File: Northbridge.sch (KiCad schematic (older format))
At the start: 25 parts, among them J301 JTAG

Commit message: Redecoupling
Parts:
- removed C301, C302, C303, C304, C305, C306, C307, C308, C309, C310, C311, C312, C313, C314, C315, C316: 1u, IPC7351-Nominal:CAPC1005X55, symbol C-0402
- added C301, C302, C303, C304, C305, C306, C307, C308, C309, C310, C311, C312, C313, C314, C315, C316, C317, C318, C319, C320, C321, C322, C323, C324, C325, C326, C327, C328, C329, C330, C331, C332, C333, C334, C335, C336, C337, C338, C339, C340, C341, C342, C343, C344, C349, C350, C351, C352, C353, C354: 100n, IPC7351-Nominal:CAPC0603X33, symbol C-0201
- added C345, C346, C347, C348: 22u, IPC7351-Nominal:CAPC2012X70, symbol C-0805
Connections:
- wire segments 613 -> 721

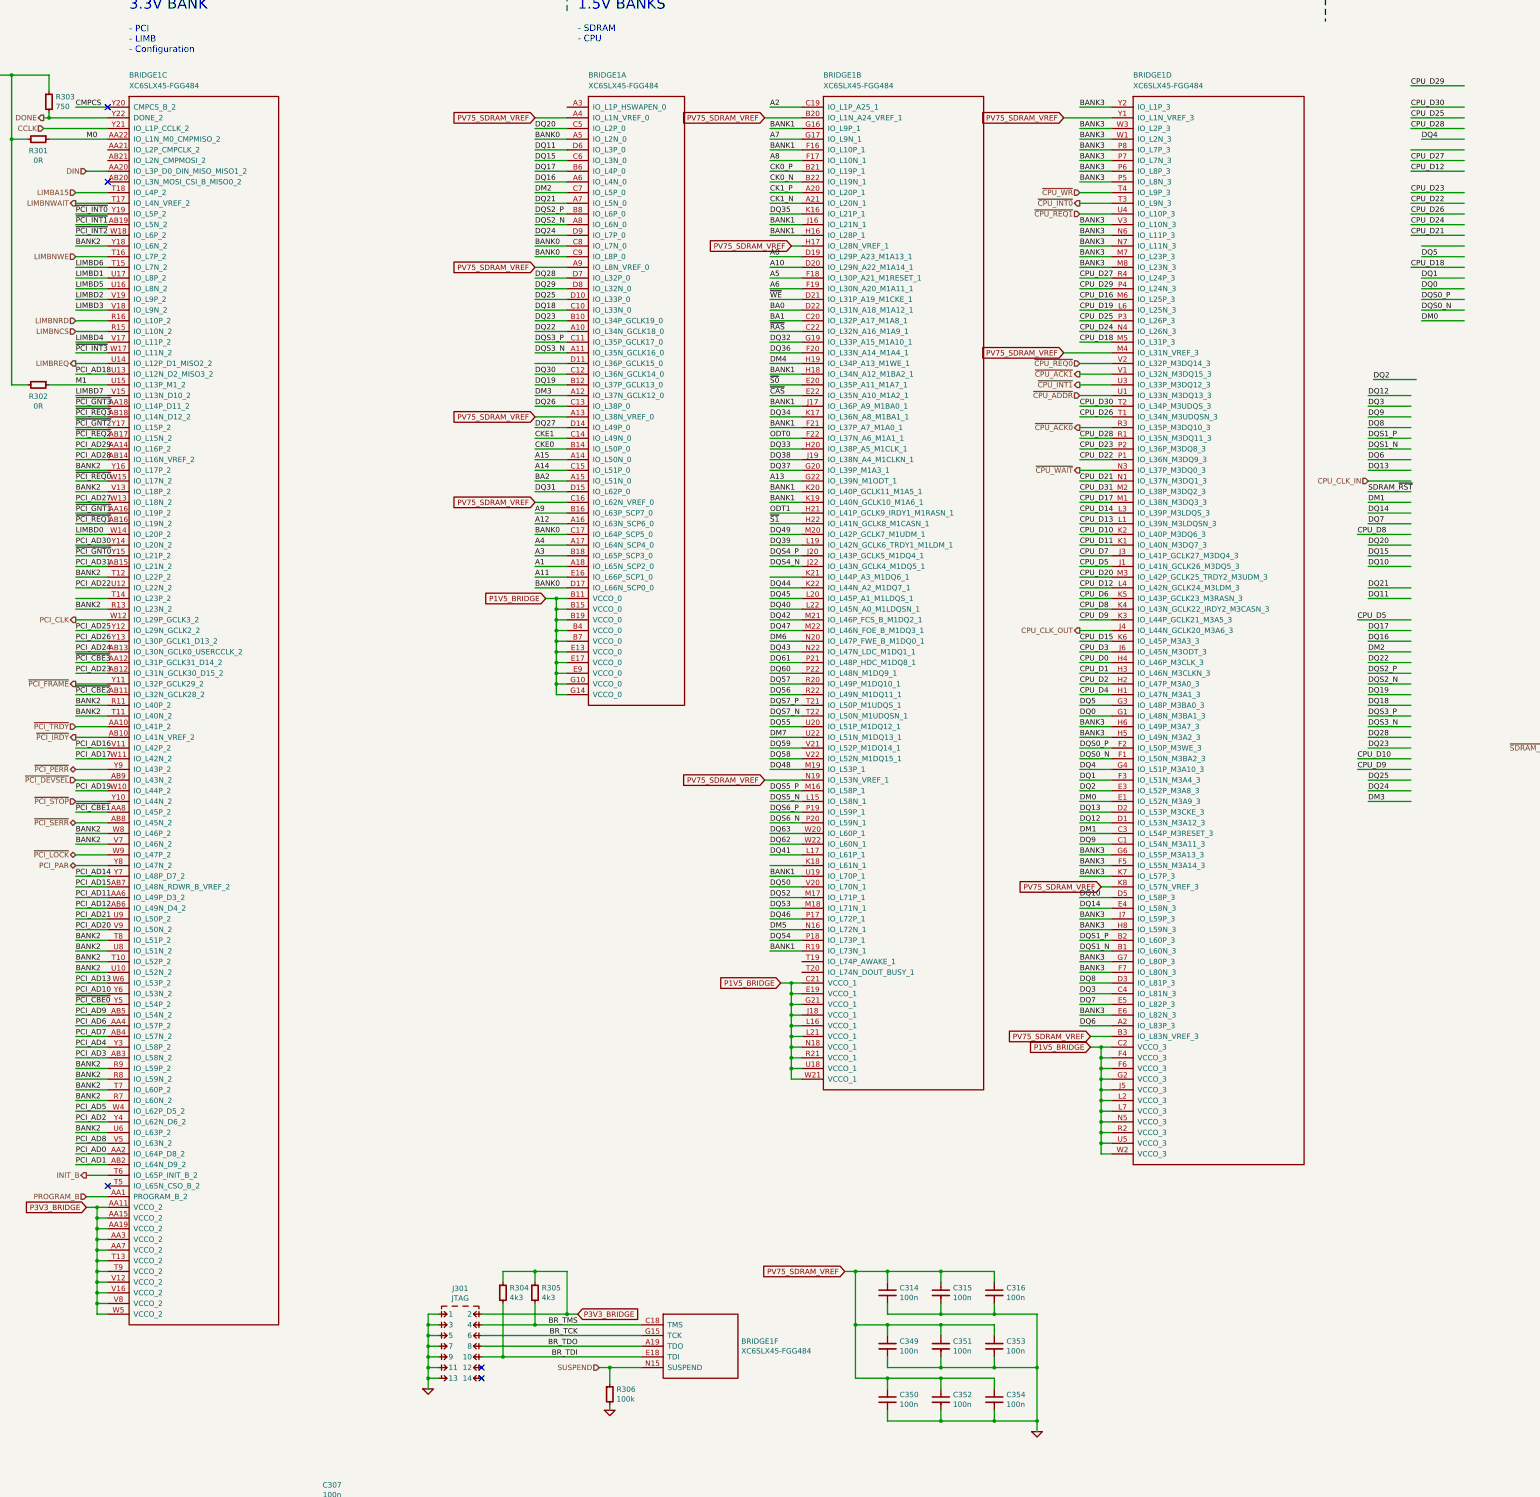
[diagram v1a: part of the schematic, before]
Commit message: Finish most redone routing
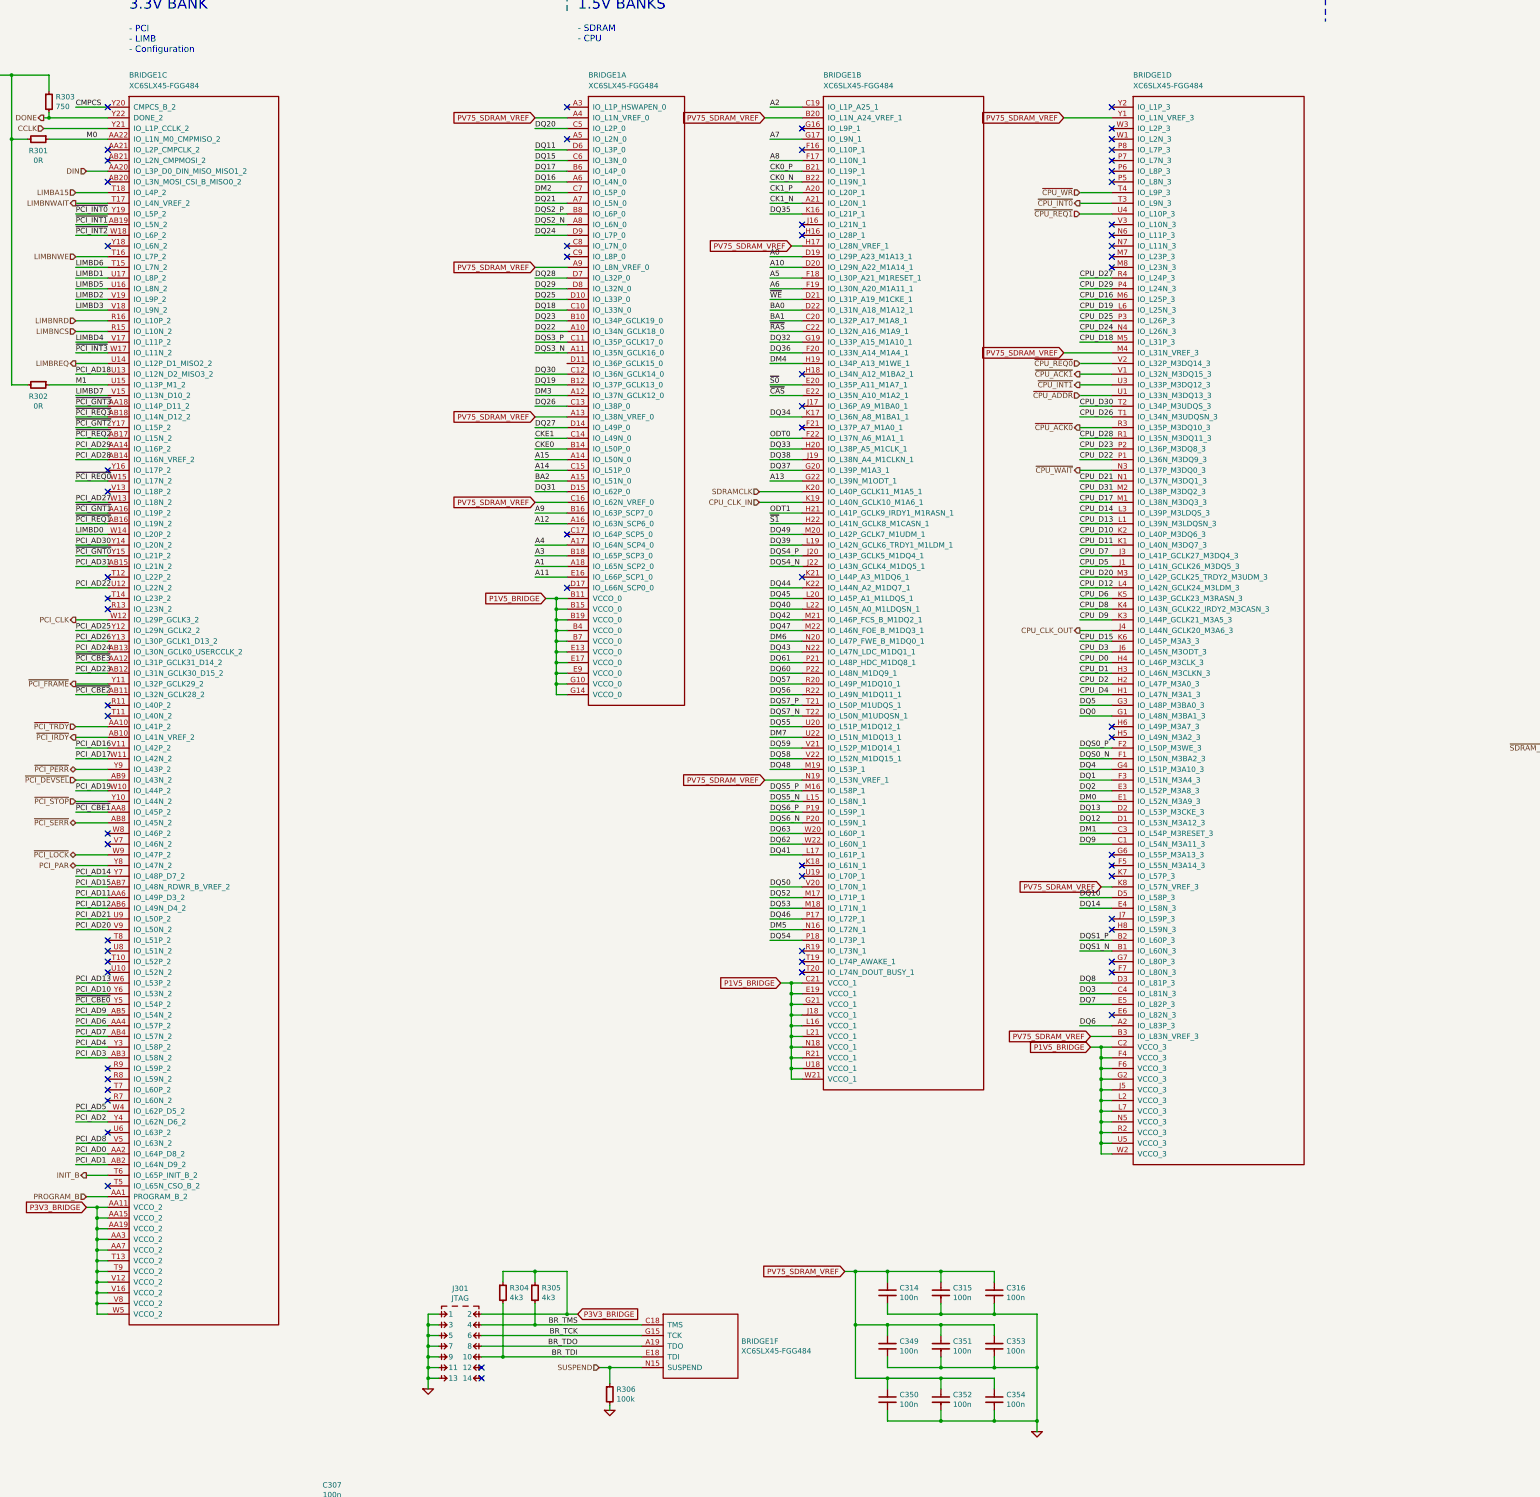
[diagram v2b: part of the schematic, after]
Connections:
- net labels added: SDRAMCLK
- net labels removed: BANK0, BANK1, BANK2, BANK3
- wire segments 721 -> 604
- no-connect marks 5 -> 67

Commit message: Fix more shit for to pass ERC
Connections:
- net SA0 is gone; now on net GND: SODIMM1.197 (SA0)
- net SA1 is gone; now on net GND: SODIMM1.201 (SA1)
- net DQ51: now also BRIDGE1.U19 (IO_L70P_1)
- net SDRAM_~RST renamed ~SDRAM_RST
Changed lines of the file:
@@
 Text Label 18000 8300 0    50   ~ 0
 ~S1
-Text Label 18000 8400 0    50   ~ 0
-SA0
-Text Label 18000 8500 0    50   ~ 0
-SA1
-Text Label 18000 8900 0    50   ~ 0
-SDRAM_~RST
 Text Label 18000 9200 0    50   ~ 0
 ODT0
@@
 P 6000 18200
 AR Path="/5763AB3B/5799D8FC" Ref="#PWR?"  Part="1"
-AR Path="/5763A638/5799D8FC" Ref="#PWR301"  Part="1"
-F 0 "#PWR301" H 6000 18200 30  0001 C CNN
+AR Path="/5763A638/5799D8FC" Ref="#PWR065"  Part="1"
+F 0 "#PWR065" H 6000 18200 30  0001 C CNN
 F 1 "GND" H 6000 18130 30  0001 C CNN
 F 2 "" H 6000 18200 60  0000 C CNN
@@
 P 7200 14800
 AR Path="/5763AB3B/57A7C581" Ref="#PWR?"  Part="1"
-AR Path="/5763A638/57A7C581" Ref="#PWR305"  Part="1"
-F 0 "#PWR305" H 7200 14800 30  0001 C CNN
+AR Path="/5763A638/57A7C581" Ref="#PWR066"  Part="1"
+F 0 "#PWR066" H 7200 14800 30  0001 C CNN
 F 1 "GND" H 7200 14730 30  0001 C CNN
 F 2 "" H 7200 14800 60  0000 C CNN
@@
 $EndComp
 $Comp
-L GND #PWR309
+L GND #PWR067
 U 1 1 57A6FC44
 P 8900 15000
-F 0 "#PWR309" H 8900 15000 30  0001 C CNN
+F 0 "#PWR067" H 8900 15000 30  0001 C CNN
 F 1 "GND" H 8900 14930 30  0001 C CNN
 F 2 "" H 8900 15000 60  0000 C CNN
@@
 	18000 8300 18500 8300
 Wire Wire Line
-	18000 8400 18500 8400
-Wire Wire Line
-	18000 8500 18500 8500
-Wire Wire Line
 	18000 9300 18500 9300
 Wire Wire Line
 	18000 9200 18500 9200
 Wire Wire Line
-	18000 8900 18500 8900
+	17900 8900 18500 8900
 Wire Notes Line
 	8500 1900 8500 1700
@@
 P 6000 19400
 AR Path="/5763AB3B/57C492A1" Ref="#PWR?"  Part="1"
-AR Path="/5763A638/57C492A1" Ref="#PWR302"  Part="1"
-F 0 "#PWR302" H 6000 19400 30  0001 C CNN
+AR Path="/5763A638/57C492A1" Ref="#PWR068"  Part="1"
+F 0 "#PWR068" H 6000 19400 30  0001 C CNN
 F 1 "GND" H 6000 19330 30  0001 C CNN
 F 2 "" H 6000 19400 60  0000 C CNN
@@
 P 6000 20600
 AR Path="/5763AB3B/57C49506" Ref="#PWR?"  Part="1"
-AR Path="/5763A638/57C49506" Ref="#PWR303"  Part="1"
-F 0 "#PWR303" H 6000 20600 30  0001 C CNN
+AR Path="/5763A638/57C49506" Ref="#PWR069"  Part="1"
+F 0 "#PWR069" H 6000 20600 30  0001 C CNN
 F 1 "GND" H 6000 20530 30  0001 C CNN
 F 2 "" H 6000 20600 60  0000 C CNN
@@
 P 8600 18200
 AR Path="/5763AB3B/57C4D6CE" Ref="#PWR?"  Part="1"
-AR Path="/5763A638/57C4D6CE" Ref="#PWR307"  Part="1"
-F 0 "#PWR307" H 8600 18200 30  0001 C CNN
+AR Path="/5763A638/57C4D6CE" Ref="#PWR070"  Part="1"
+F 0 "#PWR070" H 8600 18200 30  0001 C CNN
 F 1 "GND" H 8600 18130 30  0001 C CNN
 F 2 "" H 8600 18200 60  0000 C CNN
@@
 P 8600 19400
 AR Path="/5763AB3B/57C4DA02" Ref="#PWR?"  Part="1"
-AR Path="/5763A638/57C4DA02" Ref="#PWR308"  Part="1"
-F 0 "#PWR308" H 8600 19400 30  0001 C CNN
+AR Path="/5763A638/57C4DA02" Ref="#PWR071"  Part="1"
+F 0 "#PWR071" H 8600 19400 30  0001 C CNN
 F 1 "GND" H 8600 19330 30  0001 C CNN
 F 2 "" H 8600 19400 60  0000 C CNN
@@
 P 7900 20200
 AR Path="/5763AB3B/57C5B80A" Ref="#PWR?"  Part="1"
-AR Path="/5763A638/57C5B80A" Ref="#PWR306"  Part="1"
-F 0 "#PWR306" H 7900 20200 30  0001 C CNN
+AR Path="/5763A638/57C5B80A" Ref="#PWR072"  Part="1"
+F 0 "#PWR072" H 7900 20200 30  0001 C CNN
 F 1 "GND" H 7900 20130 30  0001 C CNN
 F 2 "" H 7900 20200 60  0000 C CNN
@@
 P 7000 20700
 AR Path="/5763AB3B/57C5BDEC" Ref="#PWR?"  Part="1"
-AR Path="/5763A638/57C5BDEC" Ref="#PWR304"  Part="1"
-F 0 "#PWR304" H 7000 20700 30  0001 C CNN
+AR Path="/5763A638/57C5BDEC" Ref="#PWR073"  Part="1"
+F 0 "#PWR073" H 7000 20700 30  0001 C CNN
 F 1 "GND" H 7000 20630 30  0001 C CNN
 F 2 "" H 7000 20700 60  0000 C CNN
@@
 Connection ~ 12500 14600
 $Comp
-L GND #PWR310
+L GND #PWR074
 U 1 1 57C62AB6
 P 12900 15200
-F 0 "#PWR310" H 12900 15200 30  0001 C CNN
+F 0 "#PWR074" H 12900 15200 30  0001 C CNN
 F 1 "GND" H 12900 15130 30  0001 C CNN
 F 2 "" H 12900 15200 60  0000 C CNN
@@
 NoConn ~ 8500 7300
 NoConn ~ 10700 9900
-NoConn ~ 10700 10000
 NoConn ~ 10700 10700
 NoConn ~ 10700 10800
@@
 Wire Wire Line
 	10700 6400 10300 6400
+Text Label 10400 10000 0    50   ~ 0
+DQ51
+Wire Wire Line
+	10700 10000 10400 10000
+$Comp
+L GND #PWR075
+U 1 1 57C95A90
+P 18400 8550
+F 0 "#PWR075" H 18400 8550 30  0001 C CNN
+F 1 "GND" H 18400 8480 30  0001 C CNN
+F 2 "" H 18400 8550 60  0000 C CNN
+F 3 "" H 18400 8550 60  0000 C CNN
+	1    18400 8550
+	1    0    0    -1
+$EndComp
+Wire Wire Line
+	18400 8550 18400 8400
+Wire Wire Line
+	18400 8400 18500 8400
+Wire Wire Line
+	18500 8500 18400 8500
+Connection ~ 18400 8500
+Text HLabel 17900 8900 0    50   Input ~ 0
+~SDRAM_RST
+NoConn ~ 8500 5200
 $EndSCHEMATC

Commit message: Fix fuckup 2: bank 0 ain't got no SSTL
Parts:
- removed C349, C350, C351, C354: 100n, IPC7351-Nominal:CAPC0603X33, symbol C-0201
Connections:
- net A1: now also BRIDGE1.E5 (IO_L82P_3); no longer BRIDGE1.A18 (IO_L65N_SCP2_0)
- net A11: now also BRIDGE1.C1 (IO_L54N_M3A11_3); no longer BRIDGE1.E16 (IO_L66P_SCP1_0)
- net A12: now also BRIDGE1.B2 (IO_L60P_3); no longer BRIDGE1.A16 (IO_L63N_SCP6_0)
- net A14: now also BRIDGE1.D2 (IO_L53P_M3CKE_3); no longer BRIDGE1.C15 (IO_L51P_0)
- net A15: now also BRIDGE1.D1 (IO_L53N_M3A12_3); no longer BRIDGE1.A14 (IO_L50N_0)
- net A3: now also BRIDGE1.E4 (IO_L58N_3); no longer BRIDGE1.B18 (IO_L65P_SCP3_0)
- net A4: now also BRIDGE1.G4 (IO_L51P_M3A10_3); no longer BRIDGE1.A17 (IO_L64N_SCP4_0)
- net A9: now also BRIDGE1.A2 (IO_L83P_3); no longer BRIDGE1.B16 (IO_L63P_SCP7_0)
- net BA2: now also BRIDGE1.B1 (IO_L60N_3); no longer BRIDGE1.A15 (IO_L51N_0)
- net CKE0: now also BRIDGE1.C3 (IO_L54P_M3RESET_3); no longer BRIDGE1.B14 (IO_L50P_0)
- net CKE1: now also BRIDGE1.E1 (IO_L52N_M3A9_3); no longer BRIDGE1.C14 (IO_L49N_0)
- net CPU_CLK_OUT: now also BRIDGE1.A9 (IO_L8N_VREF_0); no longer BRIDGE1.J4 (IO_L44N_GCLK20_M3A6_3)
- net CPU_D0: now also BRIDGE1.C11 (IO_L35P_GCLK17_0); no longer BRIDGE1.H4 (IO_L46P_M3CLK_3)
- net CPU_D1: now also BRIDGE1.A11 (IO_L35N_GCLK16_0); no longer BRIDGE1.H3 (IO_L46N_M3CLKN_3)
- net CPU_D10: now also BRIDGE1.E16 (IO_L66P_SCP1_0); no longer BRIDGE1.K2 (IO_L40P_M3DQ6_3)
- net CPU_D11: now also BRIDGE1.C15 (IO_L51P_0); no longer BRIDGE1.K1 (IO_L40N_M3DQ7_3)
- net CPU_D12: now also BRIDGE1.B8 (IO_L6P_0); no longer BRIDGE1.L4 (IO_L42N_GCLK24_M3LDM_3)
- net CPU_D13: now also BRIDGE1.A7 (IO_L5N_0); no longer BRIDGE1.L1 (IO_L39N_M3LDQSN_3)
- net CPU_D14: now also BRIDGE1.D15 (IO_L62P_0); no longer BRIDGE1.L3 (IO_L39P_M3LDQS_3)
- net CPU_D15: now also BRIDGE1.A6 (IO_L4N_0); no longer BRIDGE1.K6 (IO_L45P_M3A3_3)
- net CPU_D16: now also BRIDGE1.B6 (IO_L4P_0); no longer BRIDGE1.M6 (IO_L25P_3)
- net CPU_D17: now also BRIDGE1.A5 (IO_L2N_0); no longer BRIDGE1.M1 (IO_L38N_M3DQ3_3)
- net CPU_D18: now also BRIDGE1.A4 (IO_L1N_VREF_0); no longer BRIDGE1.M5 (IO_L31P_3)
- net CPU_D19: now also BRIDGE1.D14 (IO_L49P_0); no longer BRIDGE1.L6 (IO_L25N_3)
- net CPU_D2: now also BRIDGE1.A16 (IO_L63N_SCP6_0); no longer BRIDGE1.H2 (IO_L47P_M3A0_3)
- net CPU_D20: now also BRIDGE1.C13 (IO_L38P_0); no longer BRIDGE1.M3 (IO_L42P_GCLK25_TRDY2_M3UDM_3)
- net CPU_D21: now also BRIDGE1.A3 (IO_L1P_HSWAPEN_0); no longer BRIDGE1.N1 (IO_L37N_M3DQ1_3)
- net CPU_D22: now also BRIDGE1.D3 (IO_L81P_3); no longer BRIDGE1.P1 (IO_L36N_M3DQ9_3)
- net CPU_D23: now also BRIDGE1.D9 (IO_L7P_0); no longer BRIDGE1.P2 (IO_L36P_M3DQ8_3)
- net CPU_D24: now also BRIDGE1.C10 (IO_L33N_0); no longer BRIDGE1.N4 (IO_L26N_3)
- net CPU_D25: now also BRIDGE1.E3 (IO_L52P_M3A8_3); no longer BRIDGE1.P3 (IO_L26P_3)
- net CPU_D26: now also BRIDGE1.C8 (IO_L7N_0); no longer BRIDGE1.T1 (IO_L34N_M3UDQSN_3)
- net CPU_D27: now also BRIDGE1.D8 (IO_L32N_0); no longer BRIDGE1.R4 (IO_L24P_3)
- net CPU_D28: now also BRIDGE1.F2 (IO_L50P_M3WE_3); no longer BRIDGE1.R1 (IO_L35N_M3DQ11_3)
- net CPU_D29: now also BRIDGE1.C9 (IO_L8P_0); no longer BRIDGE1.P4 (IO_L24N_3)
- net CPU_D3: now also BRIDGE1.A10 (IO_L34N_GCLK18_0); no longer BRIDGE1.J6 (IO_L45N_M3ODT_3)
- net CPU_D30: now also BRIDGE1.K6 (IO_L45P_M3A3_3); no longer BRIDGE1.T2 (IO_L34P_M3UDQS_3)
- net CPU_D31: now also BRIDGE1.D11 (IO_L36P_GCLK15_0); no longer BRIDGE1.M2 (IO_L38P_M3DQ2_3)
- net CPU_D4: now also BRIDGE1.A15 (IO_L51N_0); no longer BRIDGE1.H1 (IO_L47N_M3A1_3)
- net CPU_D5: now also BRIDGE1.B10 (IO_L34P_GCLK19_0); no longer BRIDGE1.J1 (IO_L41N_GCLK26_M3DQ5_3)
- net CPU_D6: now also BRIDGE1.C14 (IO_L49N_0); no longer BRIDGE1.K5 (IO_L43P_GCLK23_M3RASN_3)
- net CPU_D7: now also BRIDGE1.D17 (IO_L66N_SCP0_0); no longer BRIDGE1.J3 (IO_L41P_GCLK27_M3DQ4_3)
- net CPU_D8: now also BRIDGE1.C16 (IO_L62N_VREF_0); no longer BRIDGE1.K4 (IO_L43N_GCLK22_IRDY2_M3CASN_3)
- net CPU_D9: now also BRIDGE1.A8 (IO_L6N_0); no longer BRIDGE1.K3 (IO_L44P_GCLK21_M3A5_3)
- net DM0: now also BRIDGE1.U1 (IO_L33N_M3DQ13_3); no longer BRIDGE1.E1 (IO_L52N_M3A9_3)
- net DM1: now also BRIDGE1.R4 (IO_L24P_3); no longer BRIDGE1.C3 (IO_L54P_M3RESET_3)
- net DM2: now also BRIDGE1.K2 (IO_L40P_M3DQ6_3); no longer BRIDGE1.C7 (IO_L5P_0)
- net DM3: now also BRIDGE1.H5 (IO_L49N_M3A2_3); no longer BRIDGE1.A12 (IO_L37N_GCLK12_0)
- net DQ0: now also BRIDGE1.W3 (IO_L2P_3); no longer BRIDGE1.G1 (IO_L48N_M3BA1_3)
- net DQ1: now also BRIDGE1.V1 (IO_L32N_M3DQ15_3); no longer BRIDGE1.F3 (IO_L51N_M3A4_3)
- net DQ10: now also BRIDGE1.P3 (IO_L26P_3); no longer BRIDGE1.D5 (IO_L58P_3)
- net DQ11: now also BRIDGE1.P5 (IO_L8N_3); no longer BRIDGE1.D6 (IO_L3P_0)
- net DQ12: now also BRIDGE1.U4 (IO_L10P_3); no longer BRIDGE1.D1 (IO_L53N_M3A12_3)
- net DQ13: now also BRIDGE1.U3 (IO_L33P_M3DQ12_3); no longer BRIDGE1.D2 (IO_L53P_M3CKE_3)
- net DQ14: now also BRIDGE1.P4 (IO_L24N_3); no longer BRIDGE1.E4 (IO_L58N_3)
- net DQ15: now also BRIDGE1.N4 (IO_L26N_3); no longer BRIDGE1.C6 (IO_L3N_0)
- net DQ16: now also BRIDGE1.M2 (IO_L38P_M3DQ2_3); no longer BRIDGE1.A6 (IO_L4N_0)
- net DQ17: now also BRIDGE1.L1 (IO_L39N_M3LDQSN_3); no longer BRIDGE1.B6 (IO_L4P_0)
- net DQ18: now also BRIDGE1.G1 (IO_L48N_M3BA1_3); no longer BRIDGE1.C10 (IO_L33N_0)
- net DQ19: now also BRIDGE1.F1 (IO_L50N_M3BA2_3); no longer BRIDGE1.B12 (IO_L37P_GCLK13_0)
- net DQ2: now also BRIDGE1.V2 (IO_L32P_M3DQ14_3); no longer BRIDGE1.E3 (IO_L52P_M3A8_3)
- net DQ20: now also BRIDGE1.M1 (IO_L38N_M3DQ3_3); no longer BRIDGE1.C5 (IO_L2P_0)
- net DQ21: now also BRIDGE1.K1 (IO_L40N_M3DQ7_3); no longer BRIDGE1.A7 (IO_L5N_0)
- net DQ22: now also BRIDGE1.H1 (IO_L47N_M3A1_3); no longer BRIDGE1.A10 (IO_L34N_GCLK18_0)
- net DQ23: now also BRIDGE1.H2 (IO_L47P_M3A0_3); no longer BRIDGE1.B10 (IO_L34P_GCLK19_0)
- net DQ24: now also BRIDGE1.L4 (IO_L42N_GCLK24_M3LDM_3); no longer BRIDGE1.D9 (IO_L7P_0)
- net DQ25: now also BRIDGE1.L3 (IO_L39P_M3LDQS_3); no longer BRIDGE1.D10 (IO_L33P_0)
- net DQ26: now also BRIDGE1.H3 (IO_L46N_M3CLKN_3); no longer BRIDGE1.C13 (IO_L38P_0)
- net DQ27: now also BRIDGE1.G3 (IO_L48P_M3BA0_3); no longer BRIDGE1.D14 (IO_L49P_0)
- net DQ28: now also BRIDGE1.N3 (IO_L37P_M3DQ0_3); no longer BRIDGE1.D7 (IO_L32P_0)
- net DQ29: now also BRIDGE1.M3 (IO_L42P_GCLK25_TRDY2_M3UDM_3); no longer BRIDGE1.D8 (IO_L32N_0)
- net DQ3: now also BRIDGE1.P2 (IO_L36P_M3DQ8_3); no longer BRIDGE1.C4 (IO_L81N_3)
- net DQ30: now also BRIDGE1.J4 (IO_L44N_GCLK20_M3A6_3); no longer BRIDGE1.C12 (IO_L36N_GCLK14_0)
- net DQ31: now also BRIDGE1.H4 (IO_L46P_M3CLK_3); no longer BRIDGE1.D15 (IO_L62P_0)
- net DQ4: now also BRIDGE1.W1 (IO_L2N_3); no longer BRIDGE1.G4 (IO_L51P_M3A10_3)
- net DQ5: now also BRIDGE1.V3 (IO_L10N_3); no longer BRIDGE1.G3 (IO_L48P_M3BA0_3)
- net DQ6: now also BRIDGE1.P1 (IO_L36N_M3DQ9_3); no longer BRIDGE1.A2 (IO_L83P_3)
- net DQ7: now also BRIDGE1.N1 (IO_L37N_M3DQ1_3); no longer BRIDGE1.E5 (IO_L82P_3)
- net DQ8: now also BRIDGE1.T4 (IO_L9P_3); no longer BRIDGE1.D3 (IO_L81P_3)
- net DQ9: now also BRIDGE1.T3 (IO_L9N_3); no longer BRIDGE1.C1 (IO_L54N_M3A11_3)
- net DQS0_N: now also BRIDGE1.T1 (IO_L34N_M3UDQSN_3); no longer BRIDGE1.F1 (IO_L50N_M3BA2_3)
- net DQS0_P: now also BRIDGE1.T2 (IO_L34P_M3UDQS_3); no longer BRIDGE1.F2 (IO_L50P_M3WE_3)
- net DQS1_N: now also BRIDGE1.R1 (IO_L35N_M3DQ11_3); no longer BRIDGE1.B1 (IO_L60N_3)
- net DQS1_P: now also BRIDGE1.R3 (IO_L35P_M3DQ10_3); no longer BRIDGE1.B2 (IO_L60P_3)
- net DQS2_N: now also BRIDGE1.J1 (IO_L41N_GCLK26_M3DQ5_3); no longer BRIDGE1.A8 (IO_L6N_0)
- net DQS2_P: now also BRIDGE1.J3 (IO_L41P_GCLK27_M3DQ4_3); no longer BRIDGE1.B8 (IO_L6P_0)
- net DQS3_N: now also BRIDGE1.K4 (IO_L43N_GCLK22_IRDY2_M3CASN_3); no longer BRIDGE1.A11 (IO_L35N_GCLK16_0)
- net DQS3_P: now also BRIDGE1.K5 (IO_L43P_GCLK23_M3RASN_3); no longer BRIDGE1.C11 (IO_L35P_GCLK17_0)
- net PV75_SDRAM_VREF: no longer BRIDGE1.A13 (IO_L38N_VREF_0), BRIDGE1.A4 (IO_L1N_VREF_0), BRIDGE1.A9 (IO_L8N_VREF_0), BRIDGE1.C16 (IO_L62N_VREF_0)
- net ~CPU_ACK0: now also BRIDGE1.F3 (IO_L51N_M3A4_3); no longer BRIDGE1.R3 (IO_L35P_M3DQ10_3)
- net ~CPU_ACK1: now also BRIDGE1.M5 (IO_L31P_3); no longer BRIDGE1.V1 (IO_L32N_M3DQ15_3)
- net ~CPU_ADDR: now also BRIDGE1.C7 (IO_L5P_0); no longer BRIDGE1.U1 (IO_L33N_M3DQ13_3)
- net ~CPU_INT0: now also BRIDGE1.L6 (IO_L25N_3); no longer BRIDGE1.T3 (IO_L9N_3)
- net ~CPU_INT1: now also BRIDGE1.N6 (IO_L11P_3); no longer BRIDGE1.U3 (IO_L33P_M3DQ12_3)
- net ~CPU_REQ0: now also BRIDGE1.C6 (IO_L3N_0); no longer BRIDGE1.V2 (IO_L32P_M3DQ14_3)
- net ~CPU_REQ1: now also BRIDGE1.D6 (IO_L3P_0); no longer BRIDGE1.U4 (IO_L10P_3)
- net ~CPU_WAIT: now also BRIDGE1.D10 (IO_L33P_0); no longer BRIDGE1.N3 (IO_L37P_M3DQ0_3)
- net ~CPU_WR: now also BRIDGE1.D7 (IO_L32P_0); no longer BRIDGE1.T4 (IO_L9P_3)
- no-connect marks 67 -> 71

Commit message: Tidy schematics and produce PDF
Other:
- moved on the sheet: BRIDGE1A, BRIDGE1B, BRIDGE1C, BRIDGE1D, BRIDGE1F, C301, C302, C303, C304, C305, C306, C307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

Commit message: Update for KiCad 5
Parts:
- BRIDGE1: symbol XC6SLX45-FGG484 -> Xilinx:XC6SLX45-FGG484
- C301, C302, C303, C304, C305, C306, C307, C308, C309, C310, C311, C312, C313, C314, C315, C316, C317, C318, C319, C320, C321, C322, C323, C324, C325, C326, C327, C328, C329, C330, C331, C332, C333, C334, C335, C336, C337, C338, C339, C340, C341, C342, C343, C344, C352, C353: symbol C-0201 -> pasv-cap:C-0201
- C345, C346, C347, C348: symbol C-0805 -> pasv-cap:C-0805
- J301: symbol CONN-100MIL-M-2x7-SHROUD -> conn-100mil:CONN-100MIL-M-2x7-SHROUD
- R301, R302, R303, R304, R305, R306: symbol R-0402 -> pasv-res:R-0402
- SODIMM1: symbol DDR3-SODIMM -> motherboard-rescue:DDR3-SODIMM-RESCUE-motherboard
